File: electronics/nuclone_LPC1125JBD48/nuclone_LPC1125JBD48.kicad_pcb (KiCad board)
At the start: 2 copper layers, 48.3 x 76.2 mm, 41 parts, among them J1 JTAG_2X05, J2 USB-ID, J3 nuclone_small_left, J4 nuclone_small_right, SW1 RESET, U1 MCP1702-MB, U2 LPC1114FBD48_302, Y1 12MHz

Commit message: raw placement of some components
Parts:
- added C10: 1u, SquantorRcl:C_0402, F.Cu at (92.5, 89.8)
- added C11: 1u, SquantorRcl:C_0402, F.Cu at (94.8, 86.8)
- added C12: 100n, SquantorRcl:C_0402, F.Cu at (91.4, 89.8)
- added C13: 100n, SquantorRcl:C_0402, F.Cu at (92.0, 86.8)
- added C14: 10n, SquantorRcl:C_0402, F.Cu at (78.8, 71.6)
- added D1: RED, SquantorDiodes:LED_0603_hand, F.Cu at (81.6, 71.2)
- added FB4: 600, SquantorRcl:L_0402, F.Cu at (94.5, 87.9)
- added FB5: 600, SquantorRcl:L_0402, F.Cu at (97.0, 87.7)
- added JP4: VREFP, SquantorSpecial:solder_jumper_2way_conn, B.Cu at (89.5, 90.5)
- added JP5: VREFN, SquantorSpecial:solder_jumper_2way_conn, B.Cu at (89.5, 89.2)
- added R12: 10K, SquantorRcl:R_0402_hand, F.Cu at (84.4, 71.6)
- added R13: 100, SquantorRcl:R_0402_hand, F.Cu at (81.0, 72.7)
- JP1: value reset -> RESET/PIO0_0
- JP2: value reset -> SWCLK/PIO0_10
- JP3: value SWDIO -> SWDIO/PIO1_3
- N2: value 20201114 -> 20201117
- U2: value LPC1114FBD48_302 -> LPC1125FBD48_303
- moved C5 2.20 mm to (85.1, 82.0)
- moved C8 2.20 mm to (85.1, 83.1)
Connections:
- J4 pad 13: /PIO2_10 -> /GPIO_40
- J4 pad 14: /PIO2_2 -> /GPIO_41
- J4 pad 15: /PIO0_8 -> /GPIO_42
- J4 pad 16: /PIO0_9 -> /GPIO_43
- J4 pad 17: /PIO0_10 -> /PIO2_2
- J4 pad 18: /PIO1_10 -> /PIO0_8
- J4 pad 21: /PIO2_11 -> /PIO0_9
- J4 pad 22: /PIO0_11 -> /PIO0_10
- J4 pad 23: /PIO1_0 -> /PIO1_10
- J4 pad 24: /PIO1_1 -> /PIO0_11
- J4 pad 25: /PIO1_2 -> /PIO1_0
- J4 pad 26: /PIO3_0 -> /PIO1_1
- J4 pad 27: /PIO3_1 -> /PIO1_2
- J4 pad 28: /PIO2_3 -> /PIO3_0
- J4 pad 29: /PIO1_3 -> /PIO2_3
- J4 pad 30: /PIO1_4 -> /PIO1_3
- J4 pad 31: /PIO1_11 -> /PIO1_4
- J4 pad 32: /PIO3_2 -> /PIO1_11
- SW1 pad 2: /RESET -> Net-(R13-Pad2)
- U2 pad 25: /PIO2_10 -> /PIO2_2
- U2 pad 26: /PIO2_2 -> /PIO0_8
- U2 pad 27: /PIO0_8 -> /PIO0_9
- U2 pad 28: /PIO0_9 -> /TCK
- U2 pad 29: /TCK -> /PIO1_10
- U2 pad 30: /PIO1_10 -> /PIO0_11
- U2 pad 31: /PIO2_11 -> /PIO1_0
- U2 pad 32: /PIO0_11 -> /PIO1_1
- U2 pad 33: /PIO1_0 -> /VREFP
- U2 pad 34: /PIO1_1 -> /VREFN
- U2 pad 37: /PIO3_1 -> /PIO2_3
- U2 pad 38: /PIO2_3 -> /TMS
- U2 pad 39: /TMS -> /PIO1_4
- U2 pad 40: /PIO1_4 -> /VSSA
- U2 pad 43: /PIO3_2 -> /VDDA
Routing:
- net /PIO1_7: track 29.2 -> 0.00 mm
- net /PIO1_11: track 28.1 -> 0.00 mm, vias 2 -> 0
- net /PIO1_5: track 27.7 -> 0.00 mm
- net /PIO3_3: track 27.3 -> 0.00 mm
- net /PIO3_2: track 25.6 -> 0.00 mm, vias 2 -> 0
- net /PIO1_6: track 25.2 -> 0.00 mm
- net /PIO2_10: track 24.9 -> 0.00 mm
- net /PIO0_8: track 23.9 -> 0.00 mm
- net /PIO1_3: track 23.1 -> 0.00 mm, vias 1 -> 0
- net /PIO3_1: track 22.6 -> 0.00 mm
- net /PIO0_10: track 22.4 -> 0.00 mm, vias 1 -> 0
- net /PIO2_2: track 21.5 -> 0.00 mm
- net /PIO2_11: track 21.0 -> 0.00 mm
- net /PIO1_4: track 20.9 -> 0.00 mm
- net /PIO1_0: track 20.3 -> 0.00 mm
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
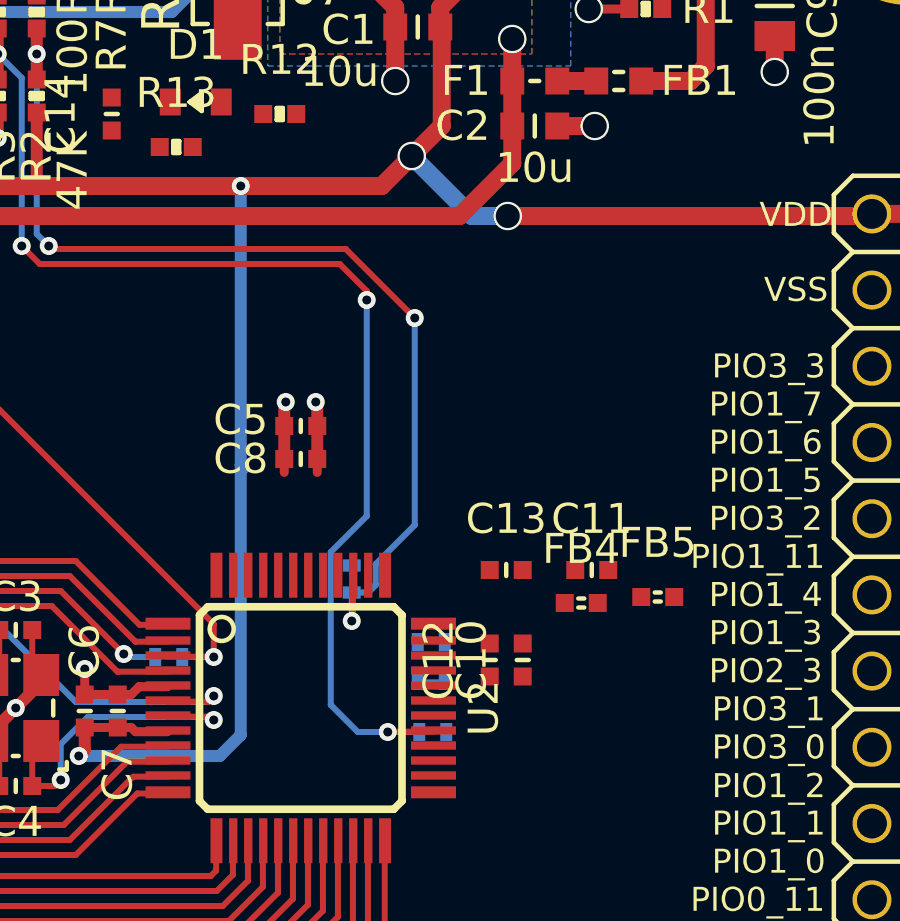
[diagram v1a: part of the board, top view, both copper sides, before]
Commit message: some bits routed, placement of components more or less done
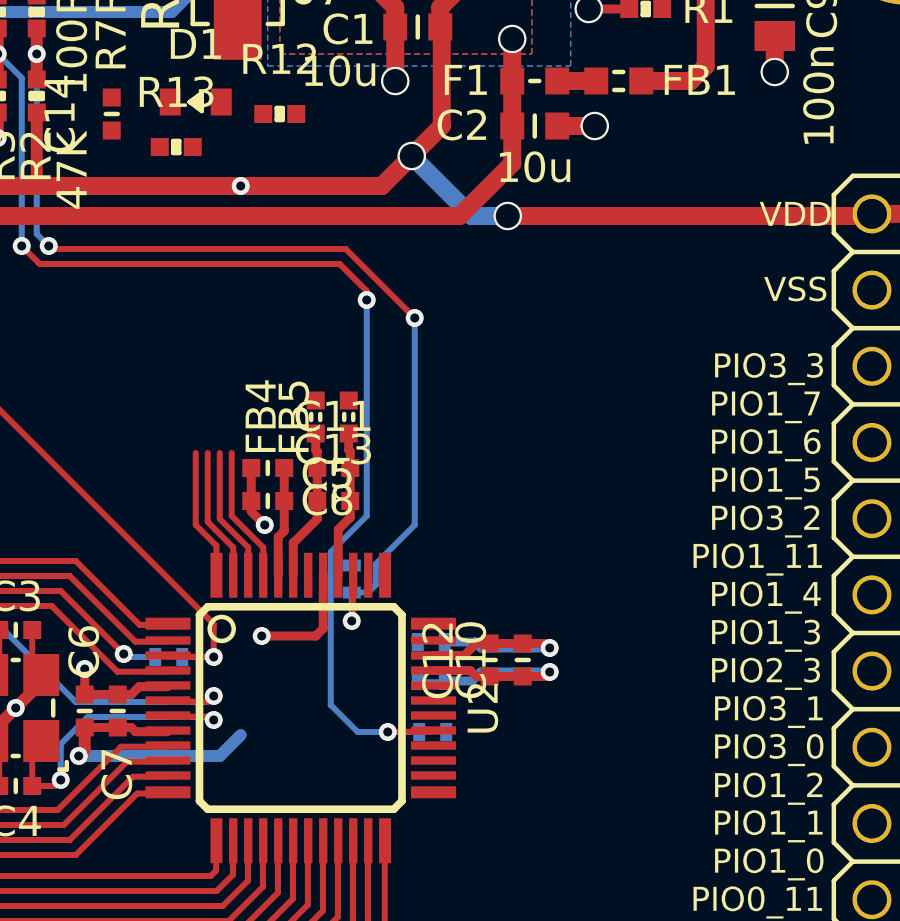
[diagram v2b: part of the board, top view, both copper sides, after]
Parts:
- moved FB5 11.9 mm to (86.7, 81.7), turned to 90 degrees
- moved FB4 10.8 mm to (85.6, 81.7), turned to 90 degrees
- moved C11 9.25 mm to (86.2, 83.4)
- moved C13 6.19 mm to (86.2, 84.5)
- moved C5 1.78 mm to (84.0, 83.4), turned to 180 degrees
- moved C8 1.78 mm to (84.0, 84.5), turned to 180 degrees
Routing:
- net /VDD: track 112.0 -> 94.8 mm, vias 5 -> 4
- net /VREFN: track 0.00 -> 7.69 mm, vias 0 -> 1
- net /VREFP: track 0.00 -> 7.64 mm, vias 0 -> 1
- net /VDDA: track 0.00 -> 5.08 mm
- net /VSSA: track 0.00 -> 4.91 mm
- net /PIO1_5: track 0.00 -> 4.51 mm
- net /PIO1_6: track 0.00 -> 4.47 mm
- net /PIO1_7: track 0.00 -> 4.43 mm
- net /PIO3_3: track 0.00 -> 4.36 mm
- net /VSS: track 26.0 -> 29.6 mm, vias 9 -> 10

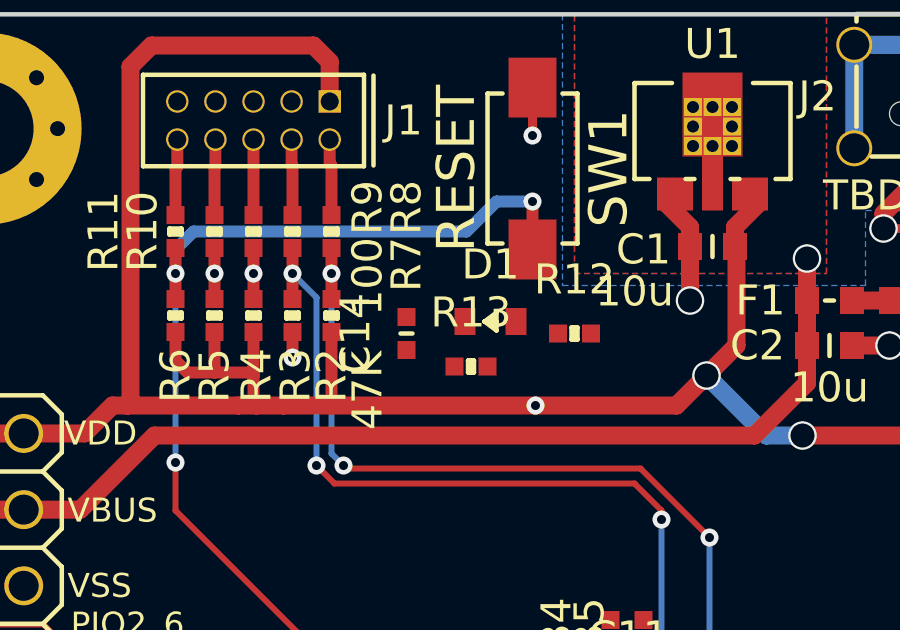
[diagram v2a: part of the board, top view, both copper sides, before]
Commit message: placed, routed, the reset led indication circuit
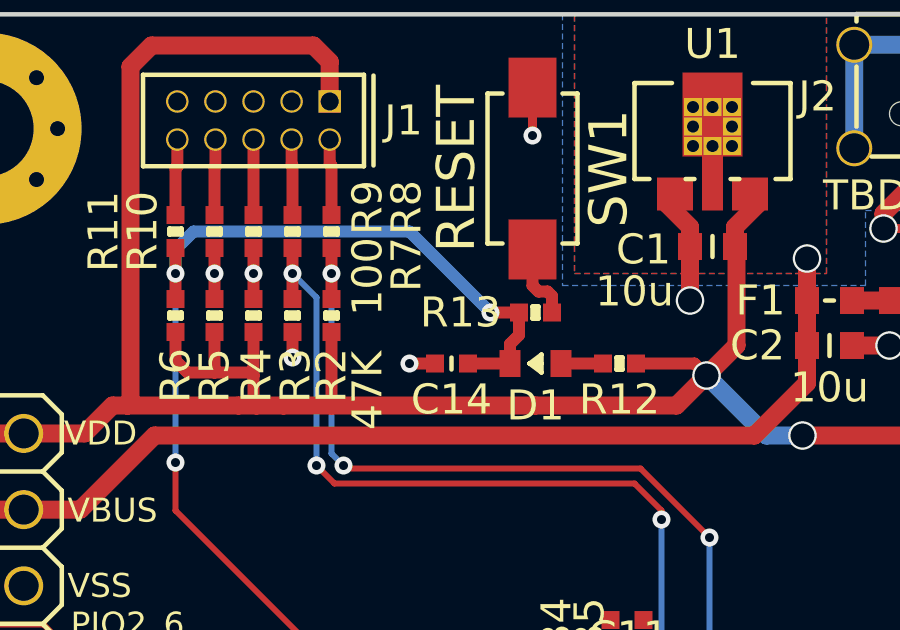
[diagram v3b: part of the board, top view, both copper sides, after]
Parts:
- moved R13 2.80 mm to (83.1, 70.9)
- moved D1 2.05 mm to (83.1, 72.6)
- moved C14 1.80 mm to (80.3, 72.6), turned to 0 degrees
- moved R12 1.80 mm to (85.9, 72.6)
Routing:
- net Net-(R13-Pad2): track 0.00 -> 2.55 mm
- net /VDD: track 94.8 -> 97.4 mm, vias 4 -> 3
- net /RESET: track 43.9 -> 45.8 mm
- net Net-(D1-Pad2): track 0.00 -> 1.40 mm
- net /VSS: track 29.6 -> 30.5 mm, vias 10 -> 11

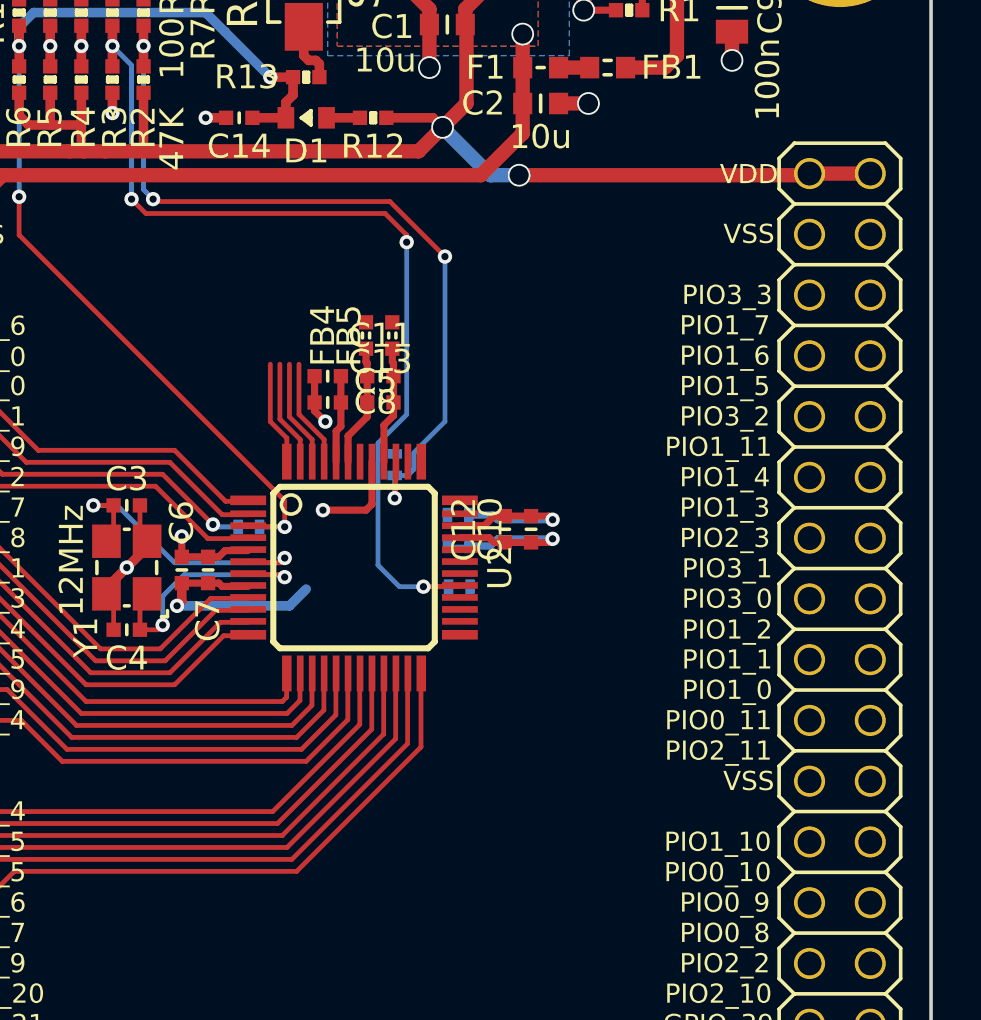
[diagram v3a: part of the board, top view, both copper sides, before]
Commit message: routed all GPIO's
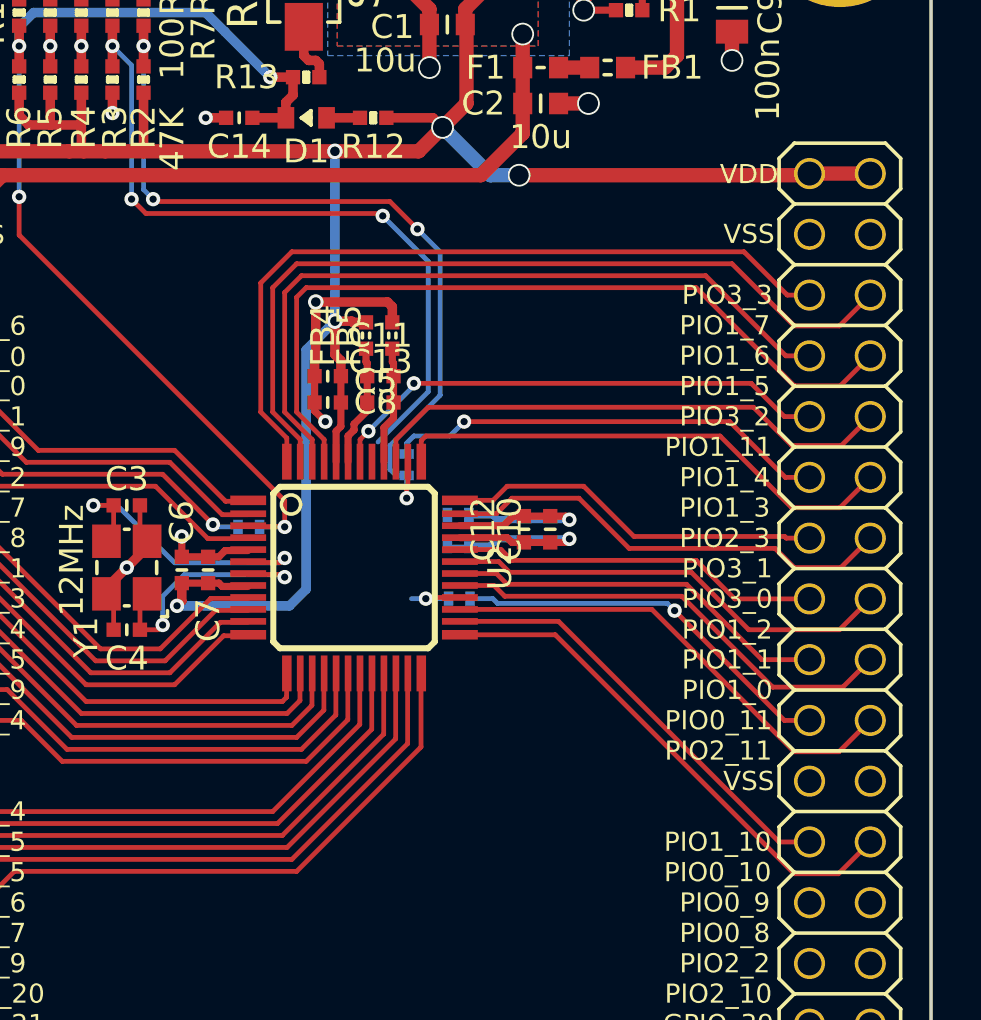
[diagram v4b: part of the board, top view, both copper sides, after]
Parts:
- moved C10 0.80 mm to (93.3, 89.8)
- moved C12 0.80 mm to (92.2, 89.8)
- moved JP2 0.50 mm to (89.5, 92.7)
- moved JP3 0.50 mm to (87.3, 87.1)
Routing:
- net /PIO1_7: track 4.43 -> 34.8 mm
- net /PIO1_5: track 4.51 -> 33.7 mm
- net /PIO3_3: track 4.36 -> 32.2 mm
- net /PIO1_6: track 4.47 -> 31.2 mm
- net /VDD: track 97.4 -> 119.9 mm, vias 3 -> 5
- net /PIO1_4: track 0.00 -> 22.5 mm
- net /PIO2_2: track 0.00 -> 21.8 mm
- net /PIO2_3: track 0.00 -> 21.5 mm
- net /PIO1_11: track 0.00 -> 21.3 mm, vias 0 -> 2
- net /PIO0_9: track 0.00 -> 20.2 mm
- net /PIO1_10: track 0.00 -> 19.4 mm
- net /PIO1_2: track 0.00 -> 19.1 mm
- net /PIO1_0: track 0.00 -> 18.9 mm
- net /PIO1_3: track 0.00 -> 18.6 mm, vias 0 -> 1
- net /PIO0_8: track 0.00 -> 18.4 mm
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
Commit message: routed all wires
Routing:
- net /VDDA: track 5.08 -> 12.5 mm, vias 0 -> 1
- net /TCK: track 33.3 -> 40.5 mm
- net /VSSA: track 4.91 -> 9.58 mm, vias 0 -> 1
- net /VSS: track 33.6 -> 35.1 mm, vias 11 -> 12
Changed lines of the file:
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@@
     (thickness 1.6)
     (drawings 8)
-    (tracks 512)
+    (tracks 529)
     (zones 0)
     (modules 53)
@@
   )
   (setup
-    (last_trace_width 0.3)
+    (last_trace_width 0.2)
     (user_trace_width 0.15)
     (user_trace_width 0.2)
@@
   (segment (start 83.5 80.3) (end 86.5 80.3) (width 0.4) (layer F.Cu) (net 11))
   (via (at 83.5 80.3) (size 0.65) (drill 0.4) (layers F.Cu B.Cu) (net 11))
+  (segment (start 85.85 86.975) (end 85.85 88.05) (width 0.3) (layer F.Cu) (net 11))
+  (via (at 85.6 88.4) (size 0.65) (drill 0.4) (layers F.Cu B.Cu) (net 11))
+  (segment (start 85.6 88.3) (end 85.6 88.4) (width 0.3) (layer F.Cu) (net 11))
+  (segment (start 85.85 88.05) (end 85.6 88.3) (width 0.3) (layer F.Cu) (net 11))
   (segment (start 72.4 66.06) (end 72.4 67.65) (width 0.4) (layer F.Cu) (net 12))
   (segment (start 72.43 66.03) (end 72.4 66.06) (width 0.4) (layer F.Cu) (net 12))
@@
   (segment (start 88.4 92.7) (end 88.45 92.65) (width 0.2) (layer F.Cu) (net 37))
   (segment (start 88.1 92.7) (end 89.05 92.7) (width 0.2) (layer B.Cu) (net 37))
-  (segment (start 88.2 84.05) (end 86.1 86.15) (width 0.2) (layer B.Cu) (net 37))
-  (segment (start 86.3 76.7) (end 88.2 78.6) (width 0.2) (layer B.Cu) (net 37))
   (segment (start 76.4 76.6) (end 75.8 76) (width 0.2) (layer F.Cu) (net 37))
-  (segment (start 87.5 92.7) (end 88.1 92.7) (width 0.2) (layer B.Cu) (net 37))
-  (segment (start 88.2 78.6) (end 88.2 84.05) (width 0.2) (layer B.Cu) (net 37))
   (segment (start 86.2 76.6) (end 76.4 76.6) (width 0.2) (layer F.Cu) (net 37))
   (segment (start 86.3 76.7) (end 86.2 76.6) (width 0.2) (layer F.Cu) (net 37))
   (via (at 86.3 76.7) (size 0.6) (drill 0.3) (layers F.Cu B.Cu) (net 37))
+  (segment (start 88.2 78.6) (end 86.3 76.7) (width 0.2) (layer B.Cu) (net 37))
+  (segment (start 88.2 84.05) (end 88.2 78.6) (width 0.2) (layer B.Cu) (net 37))
+  (segment (start 86.1 86.15) (end 88.2 84.05) (width 0.2) (layer B.Cu) (net 37))
+  (segment (start 86.1 87.5) (end 86.1 86.15) (width 0.2) (layer B.Cu) (net 37))
+  (segment (start 86.3 87.7) (end 86.1 87.5) (width 0.2) (layer B.Cu) (net 37))
+  (segment (start 86.3 91.5) (end 86.3 87.7) (width 0.2) (layer B.Cu) (net 37))
+  (segment (start 87.5 92.7) (end 86.3 91.5) (width 0.2) (layer B.Cu) (net 37))
+  (segment (start 88.1 92.7) (end 87.5 92.7) (width 0.2) (layer B.Cu) (net 37))
   (via (at 73.7 69.6) (size 0.6) (drill 0.3) (layers F.Cu B.Cu) (net 38))
   (segment (start 73.7 68.75) (end 73.7 69.6) (width 0.4) (layer F.Cu) (net 38))
@@
   (segment (start 88.2 84.7) (end 101.8 84.7) (width 0.2) (layer F.Cu) (net 73))
   (segment (start 86.85 86.975) (end 86.85 86.05) (width 0.2) (layer F.Cu) (net 73))
-  (segment (start 87.3 86.65) (end 87.3 86.2) (width 0.2) (layer B.Cu) (net 74))
-  (segment (start 87.3 86.2) (end 87.6 85.9) (width 0.2) (layer B.Cu) (net 74))
-  (via (at 89.7 85.3) (size 0.6) (drill 0.3) (layers F.Cu B.Cu) (net 74))
-  (segment (start 89.1 85.9) (end 89.7 85.3) (width 0.2) (layer B.Cu) (net 74))
-  (segment (start 87.6 85.9) (end 89.1 85.9) (width 0.2) (layer B.Cu) (net 74))
   (segment (start 103.13 87.63) (end 104.14 87.63) (width 0.2) (layer F.Cu) (net 74))
   (segment (start 100.8 85.3) (end 103.13 87.63) (width 0.2) (layer F.Cu) (net 74))
-  (segment (start 89.7 85.3) (end 100.8 85.3) (width 0.2) (layer F.Cu) (net 74))
+  (segment (start 88.6 85.3) (end 100.8 85.3) (width 0.2) (layer F.Cu) (net 74))
+  (via (at 88.6 85.3) (size 0.6) (drill 0.3) (layers F.Cu B.Cu) (net 74))
+  (segment (start 87.3 86.3) (end 87.3 86.65) (width 0.2) (layer B.Cu) (net 74))
+  (segment (start 88.3 85.3) (end 87.3 86.3) (width 0.2) (layer B.Cu) (net 74))
+  (segment (start 88.6 85.3) (end 88.3 85.3) (width 0.2) (layer B.Cu) (net 74))
   (segment (start 87.91 86.975) (end 87.91 86.09) (width 0.2) (layer F.Cu) (net 75))
   (segment (start 87.91 86.09) (end 88.1 85.9) (width 0.2) (layer F.Cu) (net 75))
@@
   (segment (start 86.35 85.55) (end 86.75 85.15) (width 0.3) (layer F.Cu) (net 83))
   (segment (start 86.35 86.975) (end 86.35 85.55) (width 0.3) (layer F.Cu) (net 83))
+  (via (at 88 89.2) (size 0.65) (drill 0.4) (layers F.Cu B.Cu) (net 83))
+  (segment (start 89 89.2) (end 88 89.2) (width 0.3) (layer B.Cu) (net 83))
+  (segment (start 88 89.2) (end 86.7 89.2) (width 0.3) (layer F.Cu) (net 83))
+  (segment (start 86.35 88.85) (end 86.35 86.975) (width 0.3) (layer F.Cu) (net 83))
+  (segment (start 86.7 89.2) (end 86.35 88.85) (width 0.3) (layer F.Cu) (net 83))
   (segment (start 85.65 84.5) (end 85.65 83.4) (width 0.3) (layer F.Cu) (net 84))
   (segment (start 85.65 83.4) (end 85.65 82.85) (width 0.3) (layer F.Cu) (net 84))
@@
   (segment (start 84.85 85.9) (end 85.1 85.65) (width 0.3) (layer F.Cu) (net 84))
   (segment (start 84.85 86.975) (end 84.85 85.9) (width 0.3) (layer F.Cu) (net 84))
+  (via (at 88 90.5) (size 0.65) (drill 0.4) (layers F.Cu B.Cu) (net 84))
+  (segment (start 89 90.5) (end 88 90.5) (width 0.3) (layer B.Cu) (net 84))
+  (segment (start 88 90.5) (end 85.2 90.5) (width 0.3) (layer F.Cu) (net 84))
+  (segment (start 84.85 90.15) (end 84.85 86.975) (width 0.3) (layer F.Cu) (net 84))
+  (segment (start 85.2 90.5) (end 84.85 90.15) (width 0.3) (layer F.Cu) (net 84))
   (segment (start 83.95 72.6) (end 85.35 72.6) (width 0.4) (layer F.Cu) (net 85))
   (segment (start 83 70) (end 83 68.79748) (width 0.4) (layer F.Cu) (net 90))
